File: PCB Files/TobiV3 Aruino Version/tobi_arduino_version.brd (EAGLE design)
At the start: 103 x 74 mm, 56 parts, among them M1 M1_M2, M2 M1_M2, M3 DF11-4PIN, M4 DF11-4PIN, M5 DF11-4PIN, M6 DF11-4PIN

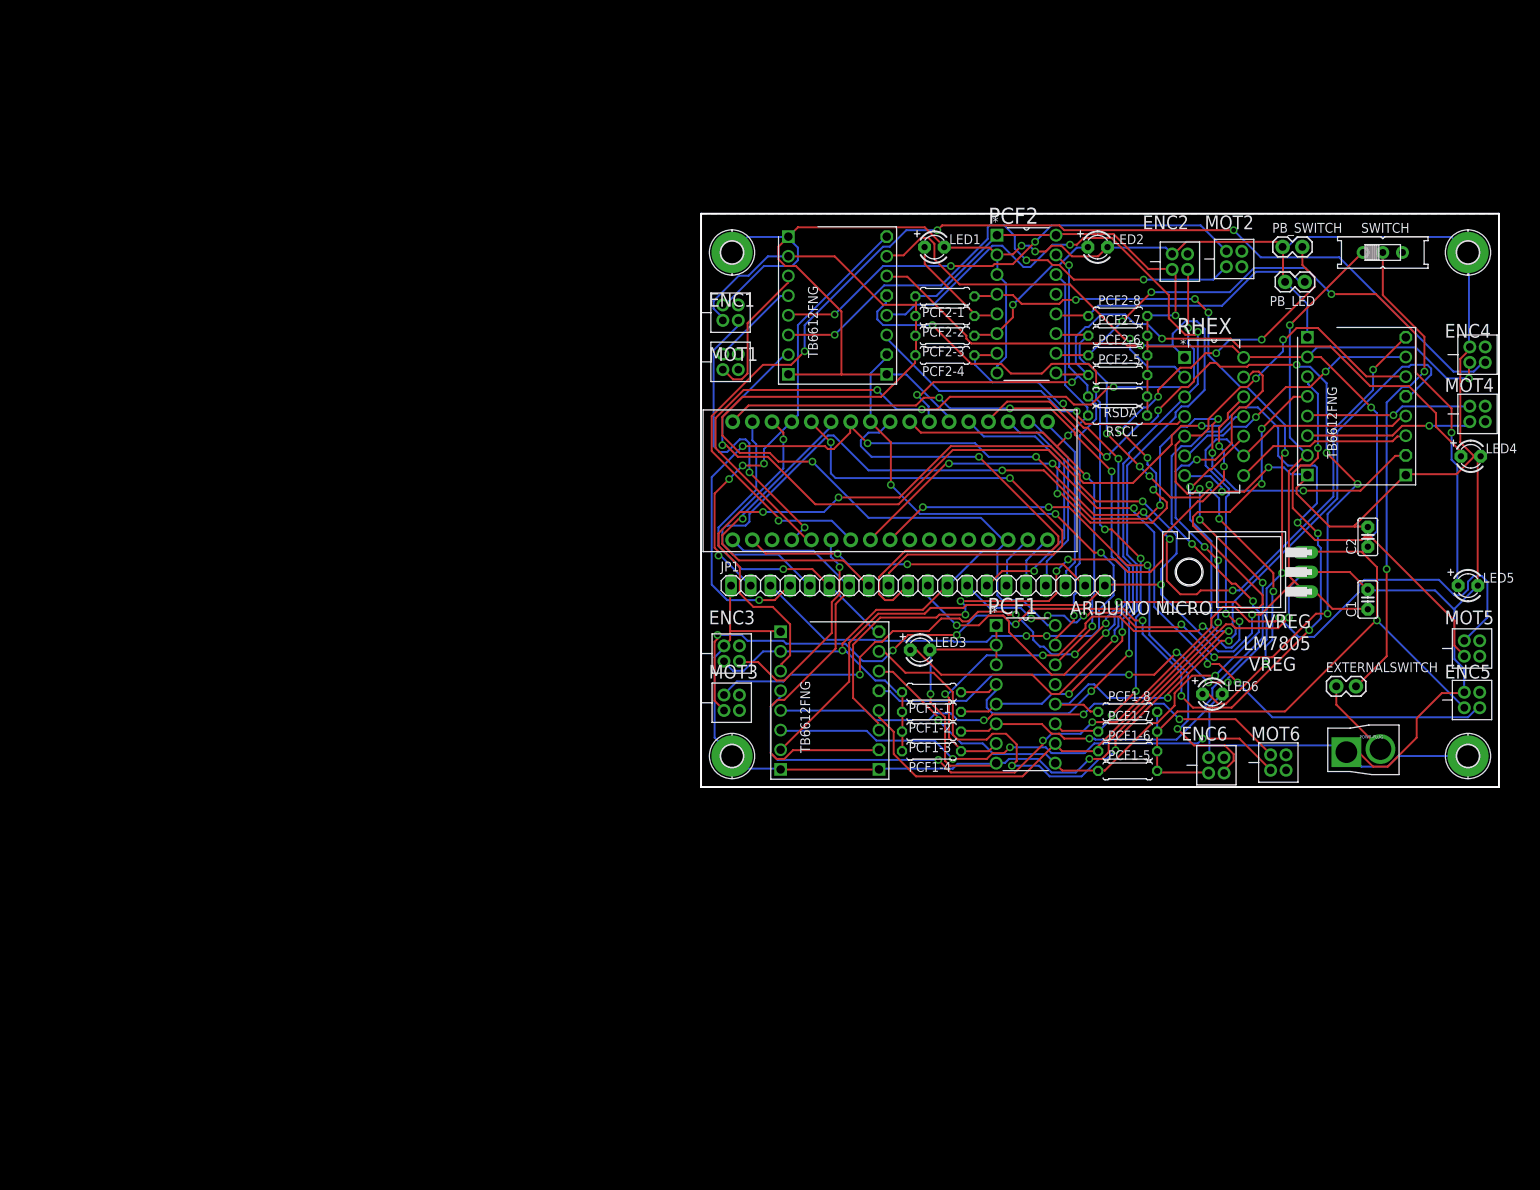
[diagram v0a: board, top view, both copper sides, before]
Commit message: removed hex encoder, moved to 0-based
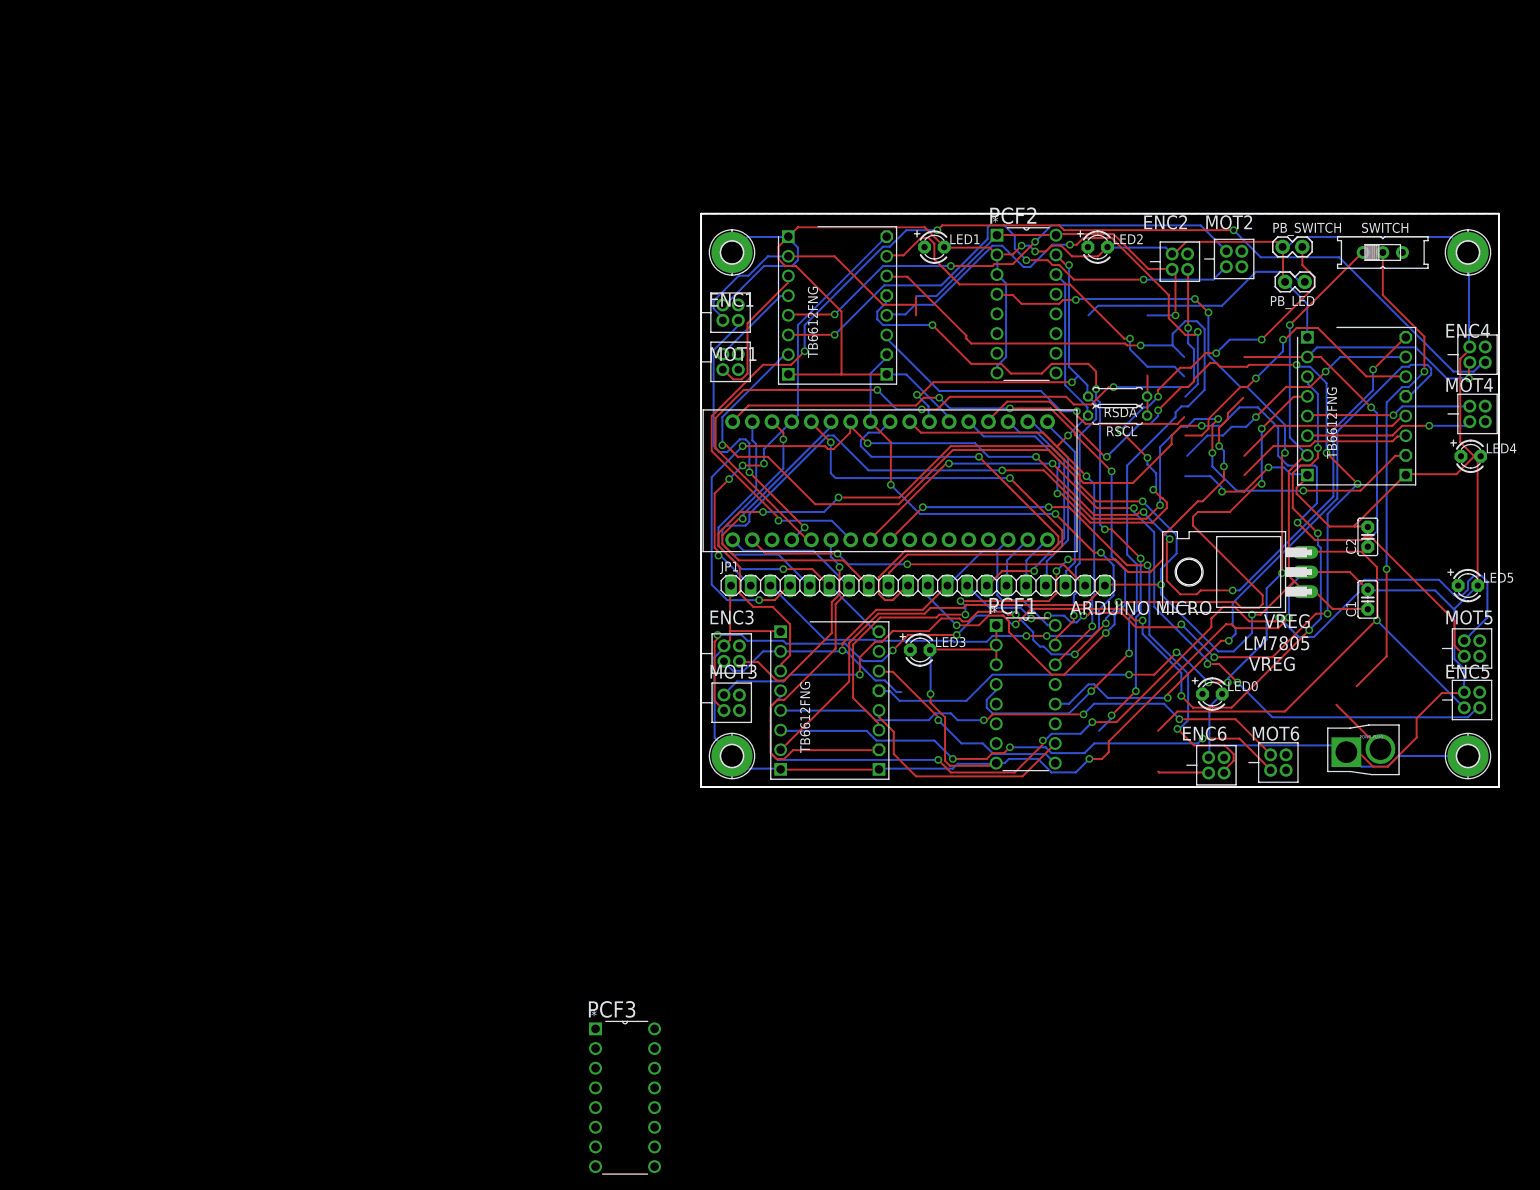
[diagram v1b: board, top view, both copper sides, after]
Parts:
- removed EXTERNALSWITCH: M02PTH, SparkFun-Connectors:1X02
- removed PCF1-1, PCF1-2, PCF1-3, PCF1-4, PCF1-5, PCF1-6, PCF1-7, PCF1-8, PCF2-1, PCF2-2, PCF2-3, PCF2-4, PCF2-5, PCF2-6, PCF2-7, PCF2-8: (no value), rcl:0207/7
- removed RHEX: SN74HC04N, Texas Instruments_By_element14_Batch_1:DIP254P762X508-14
- added PCF3: PCF8574AN, Texas Instruments_By_element14_Batch_1:DIP254P762X508-16
- renumbered LED6 to LED0
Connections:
- removed net LED6: LED0.A, PCF2-7.1, PCF2.11
- removed net M1_M2_EN: DRIVER1.STBY, PCF1-7.1, PCF1.11
- removed net M5_M6_EN: DRIVER3.STBY, PCF2-1.1, PCF2.4
- removed net M6_A: DRIVER3.BO1, M6.P1
- removed net M6_B: DRIVER3.BO2, M6.P2
- removed net M6_ENC: ARDUINOMICRO.P$26, ENC6.P3
- removed net M6_IN1: DRIVER3.BIN1, PCF1-6.1, PCF1.10, RHEX.13
- removed net M6_IN2: DRIVER3.BIN2, RHEX.12
- removed net M6_PWM: ARDUINOMICRO.P$34, DRIVER3.PWMB, JP1.7
- removed net N$3: SWITCH.S
- new net LED0: LED0.A, PCF1.10
- new net M0_A: DRIVER1.AO1, M1.P1
- new net M0_B: DRIVER1.AO2, M1.P2
- new net M0_ENC: ARDUINOMICRO.P$31, ENC1.P3
- new net M0_IN1: DRIVER1.AIN1, PCF1.4
- new net M0_IN2: DRIVER1.AIN2, PCF1.5
- new net M0_M1_EN: DRIVER1.STBY, PCF1.9
- new net M0_PWM: ARDUINOMICRO.P$4, DRIVER1.PWMA, JP1.2
- new net M2_M3_EN: PCF2.9
- new net M4_M5_EN: DRIVER3.STBY, PCF3.9
- net GND: now also PCF3.1, PCF3.3, PCF3.8, SWITCH.S; no longer RHEX.7
- net LED1: now also PCF1.11; no longer PCF2-2.1, PCF2.5
- net LED2: now also PCF2.10; no longer PCF2-3.1, PCF2.6
- net LED3: now also PCF2.11; no longer PCF2-4.1, PCF2.7
- net LED4: now also PCF3.10; no longer PCF2-5.1, PCF2.9
- net LED5: now also PCF3.11; no longer PCF2-6.1, PCF2.10
- net M1_A: now also DRIVER1.BO1, M2.P1; no longer DRIVER1.AO1, M1.P1
- net M1_B: now also DRIVER1.BO2, M2.P2; no longer DRIVER1.AO2, M1.P2
- net M1_ENC: now also ARDUINOMICRO.P$30, ENC2.P3; no longer ARDUINOMICRO.P$31, ENC1.P3
- net M1_IN1: now also DRIVER1.BIN1, PCF1.6; no longer DRIVER1.AIN1, PCF1-1.1, PCF1.4, RHEX.1
- net M1_IN2: now also DRIVER1.BIN2, PCF1.7; no longer DRIVER1.AIN2, RHEX.2
- net M1_PWM: now also ARDUINOMICRO.P$8, DRIVER1.PWMB, JP1.3; no longer ARDUINOMICRO.P$4, DRIVER1.PWMA, JP1.2
- net M2_A: now also DRIVER2.AO1, M3.P1; no longer DRIVER1.BO1, M2.P1
- net M2_B: now also DRIVER2.AO2, M3.P2; no longer DRIVER1.BO2, M2.P2
- net M2_ENC: now also ARDUINOMICRO.P$29, ENC3.P3; no longer ARDUINOMICRO.P$30, ENC2.P3
- net M2_IN1: now also DRIVER2.AIN1, PCF2.4; no longer DRIVER1.BIN1, PCF1-2.1, PCF1.5, RHEX.3
- net M2_IN2: now also DRIVER2.AIN2, PCF2.5; no longer DRIVER1.BIN2, RHEX.4
- net M2_PWM: now also ARDUINOMICRO.P$7, DRIVER2.PWMA, JP1.4; no longer ARDUINOMICRO.P$8, DRIVER1.PWMB, JP1.3
- net M3_A: now also DRIVER2.BO1, M4.P1; no longer DRIVER2.AO1, M3.P1
- net M3_B: now also DRIVER2.BO2, M4.P2; no longer DRIVER2.AO2, M3.P2
- net M3_ENC: now also ARDUINOMICRO.P$28, ENC4.P3; no longer ARDUINOMICRO.P$29, ENC3.P3
- net M3_IN1: now also DRIVER2.BIN1, PCF2.6; no longer DRIVER2.AIN1, PCF1-3.1, PCF1.6, RHEX.5
- net M3_IN2: now also DRIVER2.BIN2, PCF2.7; no longer DRIVER2.AIN2, RHEX.6
- net M3_M4_EN: no longer PCF1-8.1, PCF1.12
- net M3_PWM: now also ARDUINOMICRO.P$3, DRIVER2.PWMB, JP1.5; no longer ARDUINOMICRO.P$7, DRIVER2.PWMA, JP1.4
- net M4_A: now also DRIVER3.AO1, M5.P1; no longer DRIVER2.BO1, M4.P1
- net M4_B: now also DRIVER3.AO2, DRIVER3.BO2, M5.P2; no longer DRIVER2.BO2, M4.P2
- net M4_ENC: now also ARDUINOMICRO.P$27, ENC5.P3; no longer ARDUINOMICRO.P$28, ENC4.P3
- net M4_IN1: now also DRIVER3.AIN1, PCF3.4; no longer DRIVER2.BIN1, PCF1-4.1, PCF1.7, RHEX.9
- net M4_IN2: now also DRIVER3.AIN2, PCF3.5; no longer DRIVER2.BIN2, RHEX.8
- net M4_PWM: now also JP1.6; no longer ARDUINOMICRO.P$3, DRIVER2.PWMB, JP1.5
- net M5_A: now also DRIVER3.BO1, M6.P1; no longer DRIVER3.AO1, M5.P1
- net M5_B: now also M6.P2; no longer DRIVER3.AO2, M5.P2
- net M5_ENC: now also ARDUINOMICRO.P$26, ENC6.P3; no longer ARDUINOMICRO.P$27, ENC5.P3
- net M5_IN1: now also DRIVER3.BIN1, PCF3.6; no longer DRIVER3.AIN1, PCF1-5.1, PCF1.9, RHEX.11
- net M5_IN2: now also DRIVER3.BIN2, PCF3.7; no longer DRIVER3.AIN2, RHEX.10
- net M5_PWM: now also ARDUINOMICRO.P$34, DRIVER3.PWMB, JP1.7; no longer JP1.6
- net PB_LED: now also PCF1.12; no longer PCF2-8.1, PCF2.12
- net SCL: now also PCF3.14
- net SDA: now also PCF3.15
- net VCC: now also PCF3.16, PCF3.2; no longer ARDUINOMICRO.P$20, PCF1-1.2, PCF1-2.2, PCF1-3.2, PCF1-4.2, PCF1-5.2, PCF1-6.2, PCF1-7.2, PCF1-8.2, PCF2-1.2, PCF2-2.2, PCF2-3.2, PCF2-4.2, PCF2-5.2, PCF2-6.2, PCF2-7.2, PCF2-8.2, RHEX.14
- net V_IN: no longer EXTERNALSWITCH.1
- net V_IN_1: no longer EXTERNALSWITCH.2
- net V_MOT: now also ARDUINOMICRO.P$20
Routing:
- net M4_PWM: track 150.8 -> 0.00 mm, vias 6 -> 0
- net M5_M6_EN: track 137.0 -> 0.00 mm, vias 9 -> 0
- net M4_A: track 21.7 -> 156.9 mm, vias 1 -> 4
- net M4_M5_EN: track 0.00 -> 133.9 mm, vias 0 -> 9
- net M0_IN1: track 0.00 -> 122.4 mm, vias 0 -> 3
- net M3_A: track 141.6 -> 21.7 mm, vias 9 -> 1
- net M3_ENC: track 28.4 -> 147.8 mm, vias 1 -> 4
- net VCC: track 413.0 -> 296.9 mm, vias 6 -> 5
- net M4_B: track 21.5 -> 129.1 mm, vias 1 -> 4
- net M6_IN1: track 104.3 -> 0.00 mm, vias 4 -> 0
- net M3_B: track 122.9 -> 21.5 mm, vias 7 -> 1
- net M3_IN1: track 118.4 -> 23.0 mm, vias 6 -> 0
- net M1_M2_EN: track 93.3 -> 0.00 mm, vias 6 -> 0
- net LED5: track 89.6 -> 0.00 mm, vias 4 -> 0
- net M5_A: track 156.9 -> 68.2 mm, vias 4 -> 3
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
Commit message: moved some components around
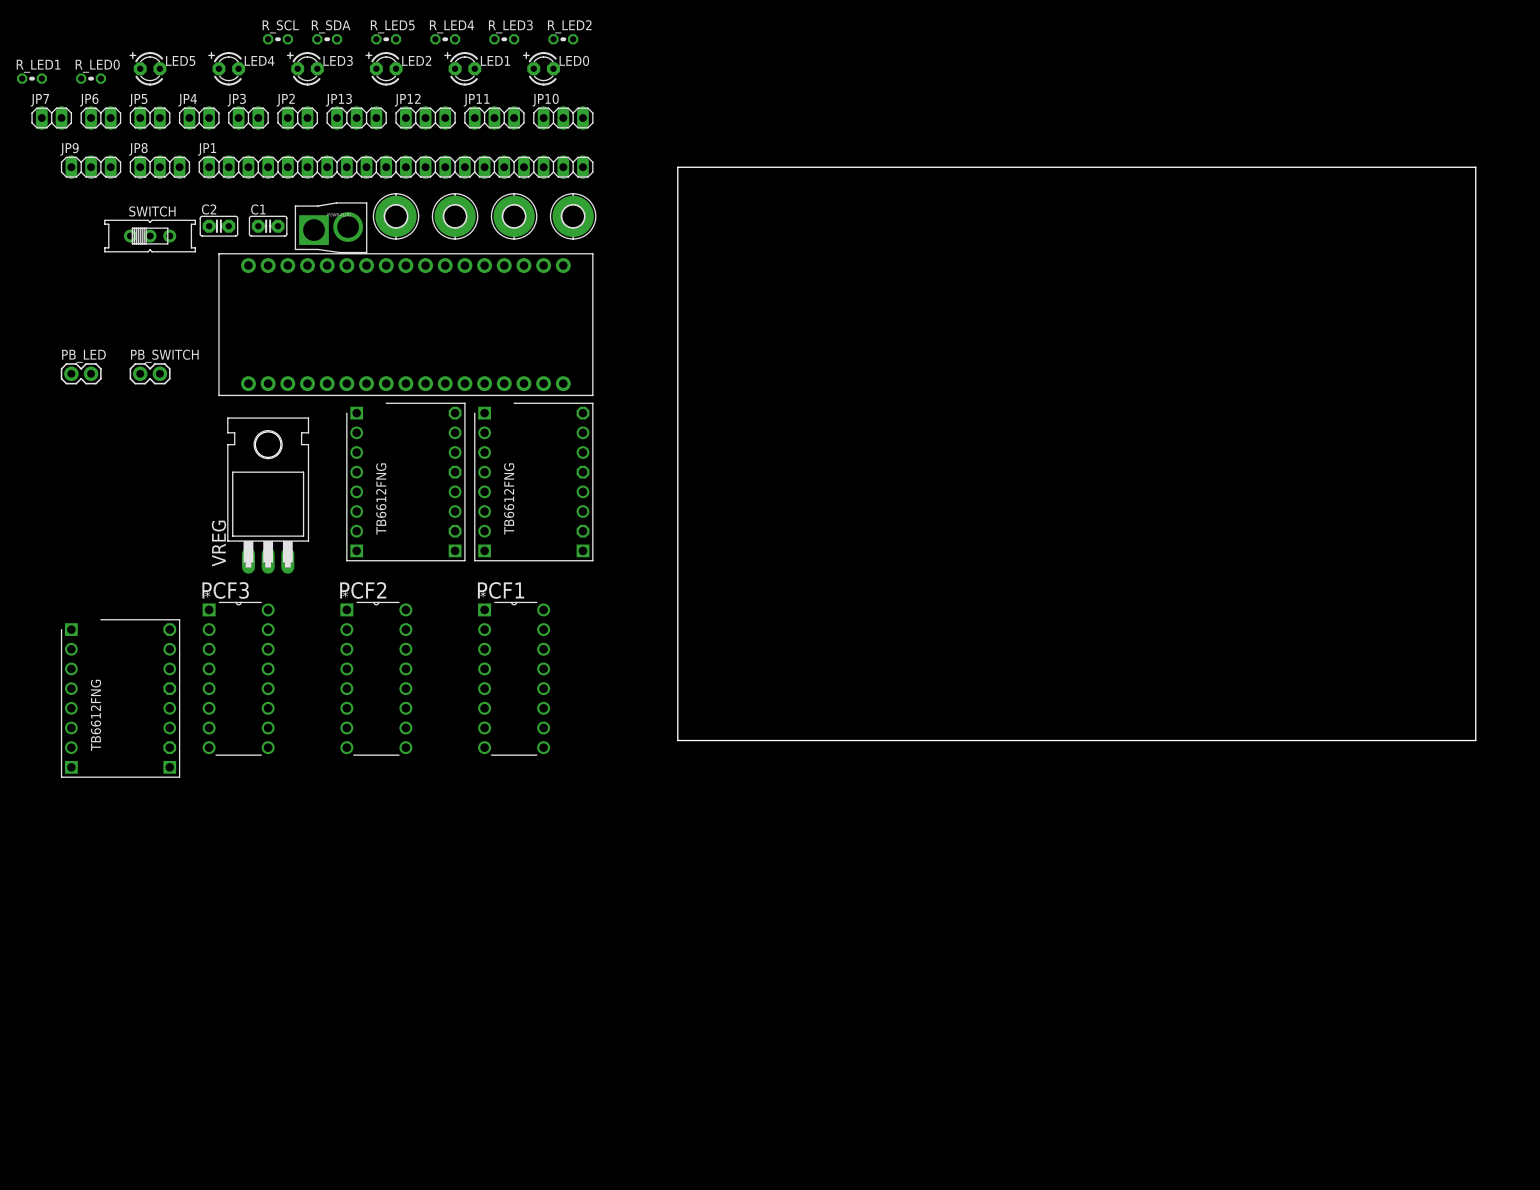
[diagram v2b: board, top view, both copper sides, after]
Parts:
- removed ENC1, ENC2, ENC3, ENC4, ENC5, ENC6, M3, M4, M5, M6: DF11-4PIN, Gavin:DF11-4PIN
- removed M1, M2: M1_M2, Gavin:DF11-4PIN
- removed RSCL, RSDA: (no value), rcl:0207/7
- added JP10, JP11, JP12, JP13, JP8, JP9: (no value), pinhead:1X03
- added JP2, JP3, JP4, JP5, JP6, JP7: (no value), pinhead:1X02
- added R_LED0, R_LED1, R_LED2, R_LED3, R_LED4, R_LED5, R_SCL, R_SDA: (no value), resistor:0204V
- moved LED5 182.7 mm to (-71.1, 92.7)
- moved LED4 167.9 mm to (-61.0, 92.7)
- moved PB_LED 159.7 mm to (-81.3, 53.3), turned to 0 degrees
- moved SWITCH 159.1 mm to (-71.1, 71.1)
- moved C2 153.6 mm to (-62.2, 72.4), turned to 0 degrees
- moved C1 149.9 mm to (-55.9, 72.4), turned to 0 degrees
- moved POWR-PLUG 149.3 mm to (-48.3, 72.4)
- moved PB_SWITCH 148.4 mm to (-72.4, 53.3)
- moved H2 141.5 mm to (-24.1, 73.7)
- moved H3 130.8 mm to (-31.8, 73.7)
- moved VREG 124.3 mm to (-55.9, 39.4), turned to 0 degrees
- moved LED0 118.2 mm to (-20.3, 92.7)
- moved LED3 109.0 mm to (-50.8, 92.7)
- moved DRIVER2 106.7 mm to (-29.2, 29.2)
- moved DRIVER1 105.5 mm to (-82.5, 1.27)
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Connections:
- removed net D12: ARDUINOMICRO.P$1, JP1.11
- removed net D4: ARDUINOMICRO.P$9, JP1.10
- new net D11: ARDUINOMICRO.P$2, JP1.10
- new net D13: ARDUINOMICRO.P$34, JP1.11
- net GND: now also JP10.2, JP11.2, JP12.2, JP13.2, JP8.2, JP9.2; no longer ENC1.P2, ENC2.P2, ENC3.P2, ENC4.P2, ENC5.P2, ENC6.P2
- net LED0: now also R_LED0.2; no longer LED0.A
- net LED1: now also R_LED1.2; no longer LED1.A
- net LED2: now also R_LED2.2; no longer LED2.A
- net LED3: now also R_LED3.2; no longer LED3.A
- net LED4: now also R_LED4.2; no longer LED4.A
- net LED5: now also R_LED5.2; no longer LED5.A
- net M0_A: now also JP2.1; no longer M1.P1
- net M0_B: now also JP2.2; no longer M1.P2
- net M0_ENC: now also JP8.3; no longer ENC1.P3
- net M0_PWM: now also ARDUINOMICRO.P$8; no longer ARDUINOMICRO.P$4
- net M1_A: now also JP3.1; no longer M2.P1
- net M1_B: now also JP3.2; no longer M2.P2
- net M1_ENC: now also JP9.3; no longer ENC2.P3
- net M1_PWM: now also ARDUINOMICRO.P$7; no longer ARDUINOMICRO.P$8
- net M2_A: now also JP4.1; no longer M3.P1
- net M2_B: now also JP4.2; no longer M3.P2
- net M2_ENC: now also JP10.3; no longer ENC3.P3
- net M2_PWM: now also ARDUINOMICRO.P$4; no longer ARDUINOMICRO.P$7
- net M3_A: now also JP5.1; no longer M4.P1
- net M3_B: now also JP5.2; no longer M4.P2
- net M3_ENC: now also JP11.3; no longer ENC4.P3
- net M4_A: now also JP6.1; no longer M5.P1
- net M4_B: now also JP6.2; no longer M5.P2
- net M4_ENC: now also JP12.3; no longer ENC5.P3
- net M4_PWM: now also ARDUINOMICRO.P$9
- net M5_A: now also JP7.1; no longer M6.P1
- net M5_B: now also JP7.2; no longer M6.P2
- net M5_ENC: now also JP13.3; no longer ENC6.P3
- net M5_PWM: now also ARDUINOMICRO.P$1; no longer ARDUINOMICRO.P$2, ARDUINOMICRO.P$34
- net SCL: now also R_SCL.2; no longer RSCL.2
- net SDA: now also R_SDA.2; no longer RSDA.2
- net VCC: now also JP10.1, JP11.1, JP12.1, JP13.1, JP8.1, JP9.1, R_SCL.1, R_SDA.1; no longer ENC1.P1, ENC2.P1, ENC3.P1, ENC4.P1, ENC5.P1, ENC6.P1, RSCL.1, RSDA.1
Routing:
- net GND: track 550.4 -> 0.00 mm, vias 7 -> 0
- net VCC: track 296.9 -> 0.00 mm, vias 5 -> 0
- net V_MOT: track 239.7 -> 0.00 mm, vias 5 -> 0
- net M4_A: track 156.9 -> 0.00 mm, vias 4 -> 0
- net M2_PWM: track 153.2 -> 0.00 mm, vias 8 -> 0
- net M3_PWM: track 150.8 -> 0.00 mm, vias 6 -> 0
- net M3_ENC: track 147.8 -> 0.00 mm, vias 4 -> 0
- net RX: track 142.1 -> 0.00 mm, vias 11 -> 0
- net M2_A: track 141.6 -> 0.00 mm, vias 9 -> 0
- net M4_M5_EN: track 133.9 -> 0.00 mm, vias 9 -> 0
- net M4_B: track 129.1 -> 0.00 mm, vias 4 -> 0
- net M2_B: track 122.9 -> 0.00 mm, vias 7 -> 0
- net M0_IN1: track 122.4 -> 0.00 mm, vias 3 -> 0
- net D12: track 109.6 -> 0.00 mm, vias 5 -> 0
- net M1_PWM: track 107.0 -> 0.00 mm, vias 5 -> 0
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- removed copper zone on layer 1, net GND
- removed copper zone on layer 16, net GND
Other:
- board text removed: "ARDUINO MICRO"
- board text removed: "ENC1"
- board text removed: "ENC2"
- board text removed: "ENC3"
- board text removed: "ENC4"
- board text removed: "ENC5"
- board text removed: "ENC6"
- board text removed: "LM7805 VREG"
- board text removed: "MOT1"
- board text removed: "MOT2"
- board text removed: "MOT3"
- board text removed: "MOT4"
- board text removed: "MOT5"
- board text removed: "MOT6"
- board text removed: "TOBI Version 3 Cherag Bhagwagar www.to3i.com"
